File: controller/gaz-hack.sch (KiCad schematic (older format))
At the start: 19 parts, among them Q1 Q_NMOS_GSD, U1 OPTO-TRANSISTOR-4

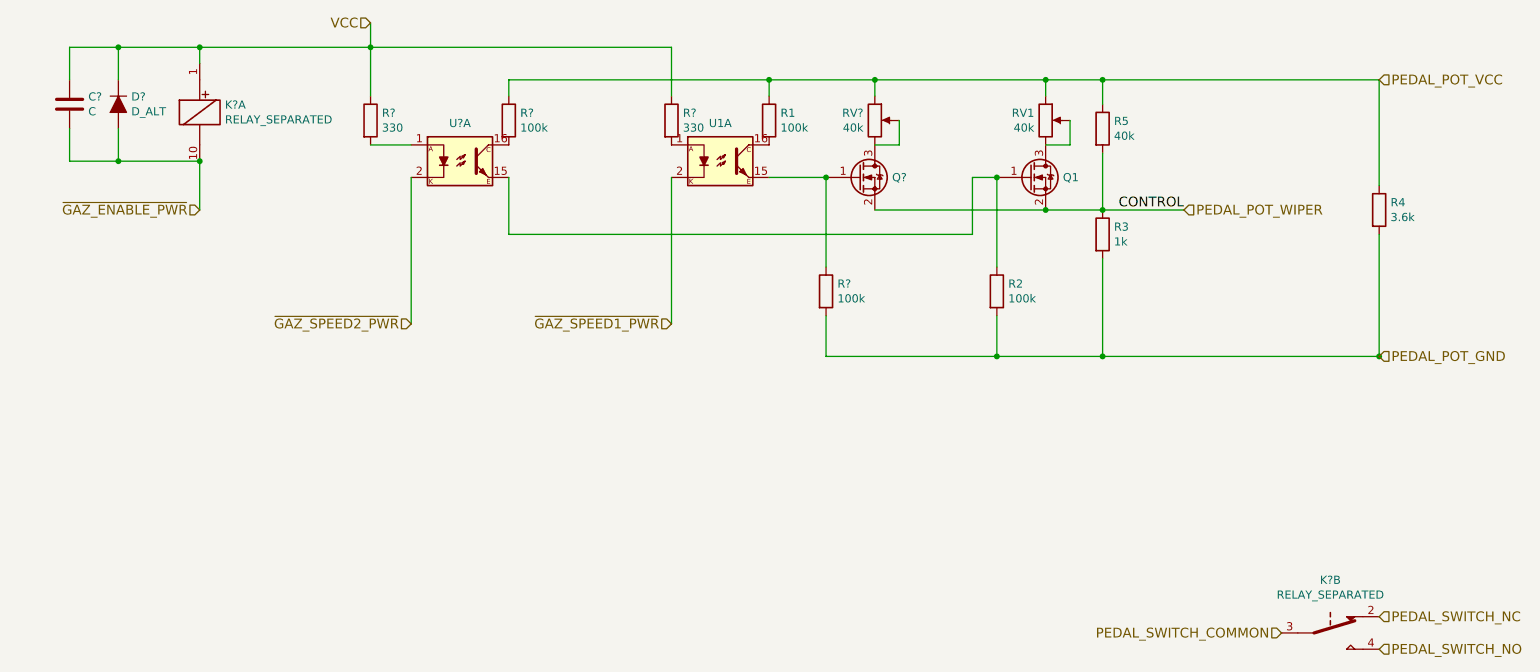
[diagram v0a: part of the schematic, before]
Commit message: Add more stuff to controller, start sourcing parts
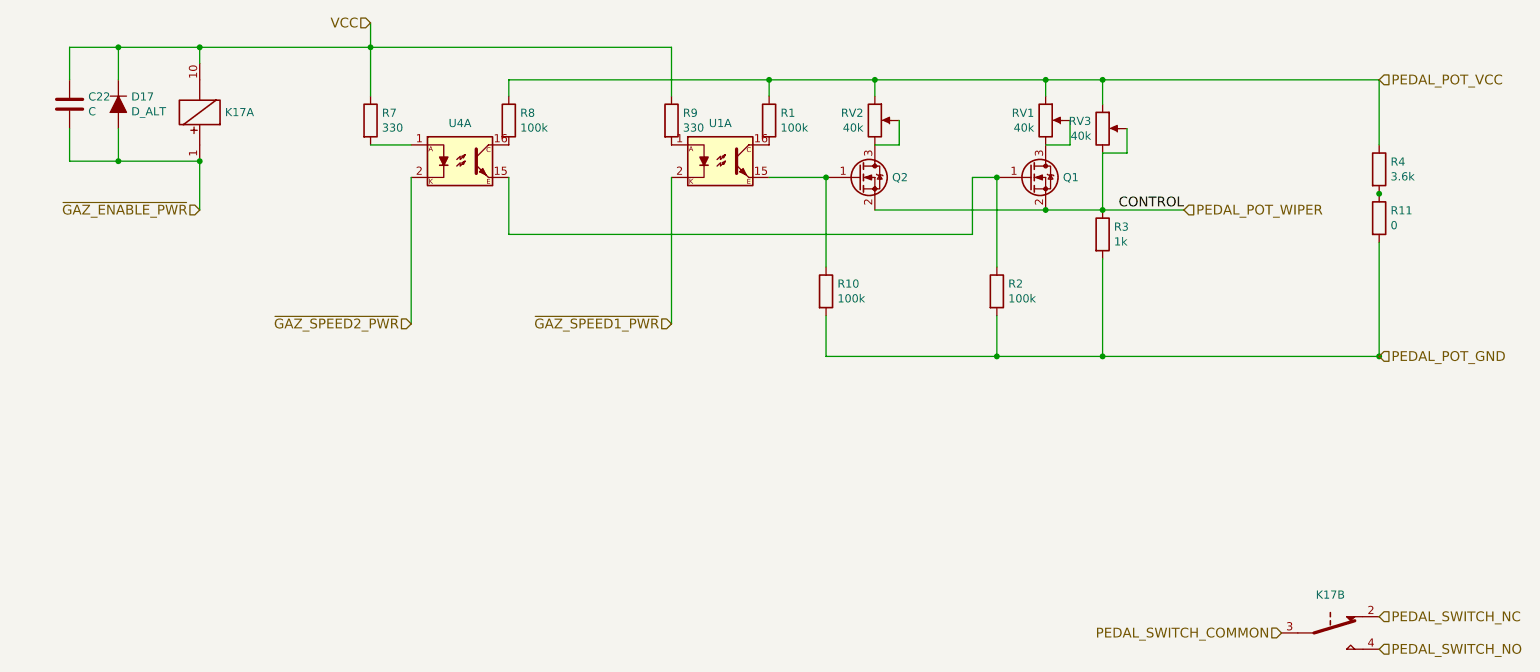
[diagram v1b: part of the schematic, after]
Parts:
- removed R5: 40k, symbol R
- added R11: 0, symbol R
- added RV3: 40k, symbol POT
- gave numbers to parts that had none: 10
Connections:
- net PEDAL_POT_GND: now also R11.2; no longer R4.2
- net PEDAL_POT_VCC: now also RV3.1
- net PEDAL_POT_WIPER: now also RV3.2, RV3.3
- net PEDAL_SWITCH_COMMON: now also K17.3; no longer K17.3
- net PEDAL_SWITCH_NC: now also K17.2; no longer K17.2
- net PEDAL_SWITCH_NO: now also K17.4; no longer K17.4
- net VCC: now also K17.10; no longer K17.1
- net ~GAZ_ENABLE_PWR: now also K17.1; no longer K17.10
- new net: R11.1, R4.2
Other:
- moved on the sheet: R4
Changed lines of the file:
@@
 LIBS:mic-parts
 LIBS:controller-cache
-LIBS:line-interface-cache
 EELAYER 26 0
 EELAYER END
 $Descr A4 11693 8268
 encoding utf-8
-Sheet 3 6
+Sheet 6 10
 Title ""
 Date ""
@@
 L R R4
 U 1 1 58BEE596
-P 9950 2400
-F 0 "R4" H 10020 2446 50  0000 L CNN
-F 1 "3.6k" H 10020 2355 50  0000 L CNN
-F 2 "" V 5480 -500 50  0001 C CNN
-F 3 "" H 5550 -500 50  0001 C CNN
-	1    9950 2400
-	1    0    0    -1
-$EndComp
-Wire Wire Line
-	9950 1600 9950 2250
-Wire Wire Line
-	9950 3300 9950 2550
+P 9950 2150
+F 0 "R4" H 10020 2196 50  0000 L CNN
+F 1 "3.6k" H 10020 2105 50  0000 L CNN
+F 2 "" V 5480 -750 50  0001 C CNN
+F 3 "" H 5550 -750 50  0001 C CNN
+	1    9950 2150
+	1    0    0    -1
+$EndComp
+Wire Wire Line
+	9950 1600 9950 2000
 $Comp
 L OPTO-TRANSISTOR-4 U1
@@
 Connection ~ 7900 1600
 Connection ~ 7600 2200
-$Comp
-L R R5
-U 1 1 58BEEDC4
-P 8250 1900
-F 0 "R5" H 8320 1946 50  0000 L CNN
-F 1 "40k" H 8320 1855 50  0000 L CNN
-F 2 "" V 3780 -1000 50  0001 C CNN
-F 3 "" H 3850 -1000 50  0001 C CNN
-	1    8250 1900
-	1    0    0    -1
-$EndComp
 Wire Wire Line
 	8250 1750 8250 1600
@@
 Connection ~ 8250 3300
 $Comp
-L Q_NMOS_GSD Q?
+L Q_NMOS_GSD Q2
 U 1 1 58C00A06
 P 6750 2200
-F 0 "Q?" H 6956 2200 50  0000 L CNN
+F 0 "Q2" H 6956 2200 50  0000 L CNN
 F 1 "Q_NMOS_GSD" H 6955 2155 50  0001 L CNN
 F 2 "" H 2950 -400 50  0001 C CNN
@@
 $EndComp
 $Comp
-L POT RV?
+L POT RV2
 U 1 1 58C00A0C
 P 6850 1850
-F 0 "RV?" H 6780 1896 50  0000 R CNN
+F 0 "RV2" H 6780 1896 50  0000 R CNN
 F 1 "40k" H 6780 1805 50  0000 R CNN
 F 2 "" H 2700 -450 50  0001 C CNN
@@
 	6850 1600 6850 1700
 $Comp
-L R R?
+L R R10
 U 1 1 58C00A17
 P 6550 2900
-F 0 "R?" H 6620 2946 50  0000 L CNN
+F 0 "R10" H 6620 2946 50  0000 L CNN
 F 1 "100k" H 6620 2855 50  0000 L CNN
 F 2 "" V 2080 0   50  0001 C CNN
@@
 Connection ~ 7600 3300
 $Comp
-L OPTO-TRANSISTOR-4 U?
+L OPTO-TRANSISTOR-4 U4
 U 1 1 58C01026
 P 4300 2100
-F 0 "U?" H 4300 2333 50  0000 C CNN
+F 0 "U4" H 4300 2333 50  0000 C CNN
 F 1 "OPTO-TRANSISTOR-4" H 4300 2334 50  0001 C CNN
 F 2 "" H -350 -1050 50  0001 L CIN
@@
 $EndComp
 $Comp
-L R R?
+L R R8
 U 1 1 58C01078
 P 4600 1850
-F 0 "R?" H 4670 1896 50  0000 L CNN
+F 0 "R8" H 4670 1896 50  0000 L CNN
 F 1 "100k" H 4670 1805 50  0000 L CNN
 F 2 "" V 130 -1050 50  0001 C CNN
@@
 PEDAL_SWITCH_NO
 $Comp
-L RELAY_SEPARATED K?
-U 1 1 58C01F4B
-P 2700 1800
-F 0 "K?" H 2855 1846 50  0000 L CNN
-F 1 "RELAY_SEPARATED" H 2855 1755 50  0000 L CNN
-F 2 "" H -4950 -2500 50  0000 C CNN
-F 3 "" H -4950 -2500 50  0000 C CNN
-	1    2700 1800
-	1    0    0    -1
-$EndComp
-$Comp
-L RELAY_SEPARATED K?
-U 2 1 58C01FFF
+L RELAY_SEPARATED K17
+U 2 1 58C01F4B
 P 9650 5000
-F 0 "K?" V 9325 5000 50  0000 C CNN
-F 1 "RELAY_SEPARATED" V 9416 5000 50  0000 C CNN
-F 2 "" H 4550 400 50  0000 C CNN
-F 3 "" H 4550 400 50  0000 C CNN
-F 4 "?" H 9650 5000 60  0001 C CNN "PartNo"
-F 5 "?" H 9650 5000 60  0001 C CNN "Manufacturer"
-F 6 "?" H 9650 5000 60  0001 C CNN "Distributor"
+F 0 "K17" V 9416 5000 50  0000 C CNN
+F 1 "RELAY_SEPARATED" H 9805 4955 50  0001 L CNN
+F 2 "" H 2000 700 50  0000 C CNN
+F 3 "" H 2000 700 50  0000 C CNN
 	2    9650 5000
 	0    1    1    0
 $EndComp
+$Comp
+L RELAY_SEPARATED K17
+U 1 1 58C01FFF
+P 2700 1800
+F 0 "K17" H 2545 1800 50  0000 R CNN
+F 1 "RELAY_SEPARATED" V 2466 1800 50  0001 C CNN
+F 2 "" H -2400 -2800 50  0000 C CNN
+F 3 "" H -2400 -2800 50  0000 C CNN
+F 4 "?" H 2700 1800 60  0001 C CNN "PartNo"
+F 5 "?" H 2700 1800 60  0001 C CNN "Manufacturer"
+F 6 "?" H 2700 1800 60  0001 C CNN "Distributor"
+	1    2700 1800
+	-1   0    0    1
+$EndComp
 Text HLabel 4000 3100 0    60   Input ~ 0
 ~GAZ_SPEED2_PWR
@@
 Connection ~ 3750 1400
 $Comp
-L R R?
+L R R7
 U 1 1 58C023B7
 P 3750 1850
-F 0 "R?" H 3820 1896 50  0000 L CNN
+F 0 "R7" H 3820 1896 50  0000 L CNN
 F 1 "330" H 3820 1805 50  0000 L CNN
 F 2 "" V -720 -1050 50  0001 C CNN
@@
 $EndComp
 $Comp
-L R R?
+L R R9
 U 1 1 58C024A6
 P 5600 1850
-F 0 "R?" H 5670 1896 50  0000 L CNN
+F 0 "R9" H 5670 1896 50  0000 L CNN
 F 1 "330" H 5670 1805 50  0000 L CNN
 F 2 "" V 1130 -1050 50  0001 C CNN
@@
 	3750 1250 3750 1700
 $Comp
-L D_ALT D?
+L D_ALT D17
 U 1 1 58C0A9F4
 P 2200 1750
-F 0 "D?" V 2154 1671 50  0000 R CNN
+F 0 "D17" V 2154 1671 50  0000 R CNN
 F 1 "D_ALT" V 2245 1671 50  0000 R CNN
 F 2 "" H -2700 -550 50  0001 C CNN
@@
 Connection ~ 2700 2100
 $Comp
-L C C?
+L C C22
 U 1 1 58C0ABFE
 P 1900 1750
-F 0 "C?" H 2015 1796 50  0000 L CNN
+F 0 "C22" H 2015 1796 50  0000 L CNN
 F 1 "C" H 2015 1705 50  0000 L CNN
 F 2 "" H -62 -200 50  0001 C CNN
@@
 Connection ~ 2200 2100
 Connection ~ 2200 1400
+$Comp
+L POT RV3
+U 1 1 58C42214
+P 8250 1900
+F 0 "RV3" H 8180 1946 50  0000 R CNN
+F 1 "40k" H 8180 1855 50  0000 R CNN
+F 2 "" H 4100 -400 50  0001 C CNN
+F 3 "" H 4100 -400 50  0001 C CNN
+	1    8250 1900
+	1    0    0    -1
+$EndComp
+Wire Wire Line
+	8250 2050 8400 2050
+Wire Wire Line
+	8400 2050 8400 1900
+$Comp
+L R R11
+U 1 1 58C42979
+P 9950 2450
+F 0 "R11" H 10020 2496 50  0000 L CNN
+F 1 "0" H 10020 2405 50  0000 L CNN
+F 2 "" V 5480 -450 50  0001 C CNN
+F 3 "" H 5550 -450 50  0001 C CNN
+	1    9950 2450
+	1    0    0    -1
+$EndComp
+Wire Wire Line
+	9950 3300 9950 2600
+Connection ~ 9950 2300
 $EndSCHEMATC

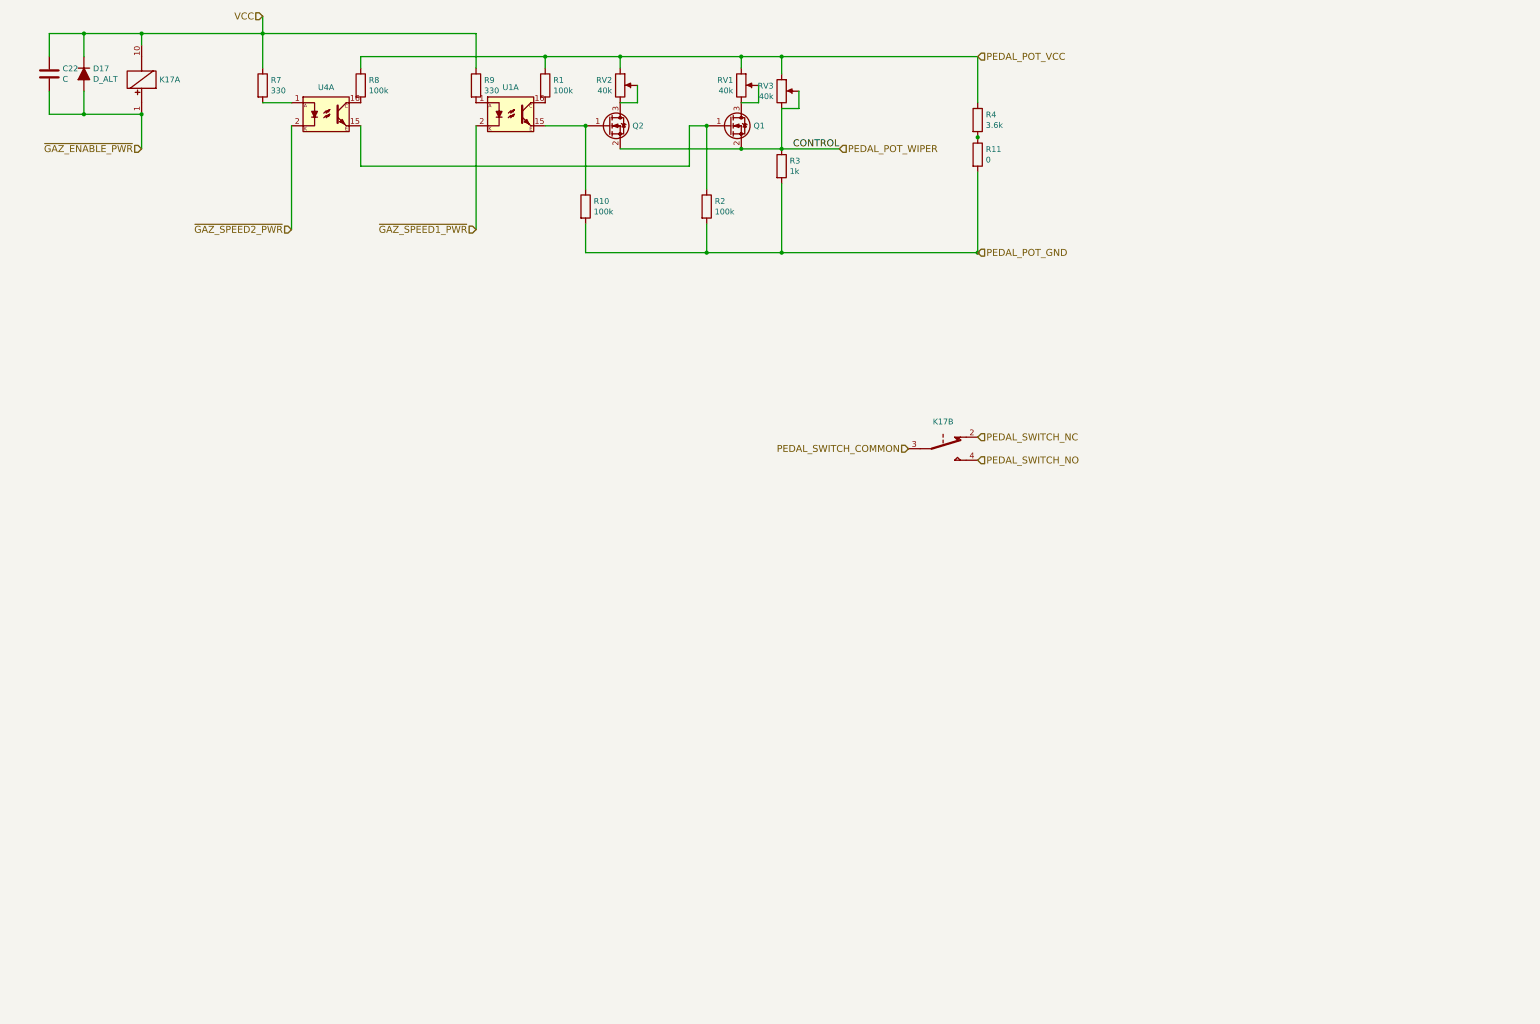
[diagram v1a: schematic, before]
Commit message: Change gas pedal interface so that it supports going up and down from the middle voltage so that it's compatible with Linde forklift gas mechanism
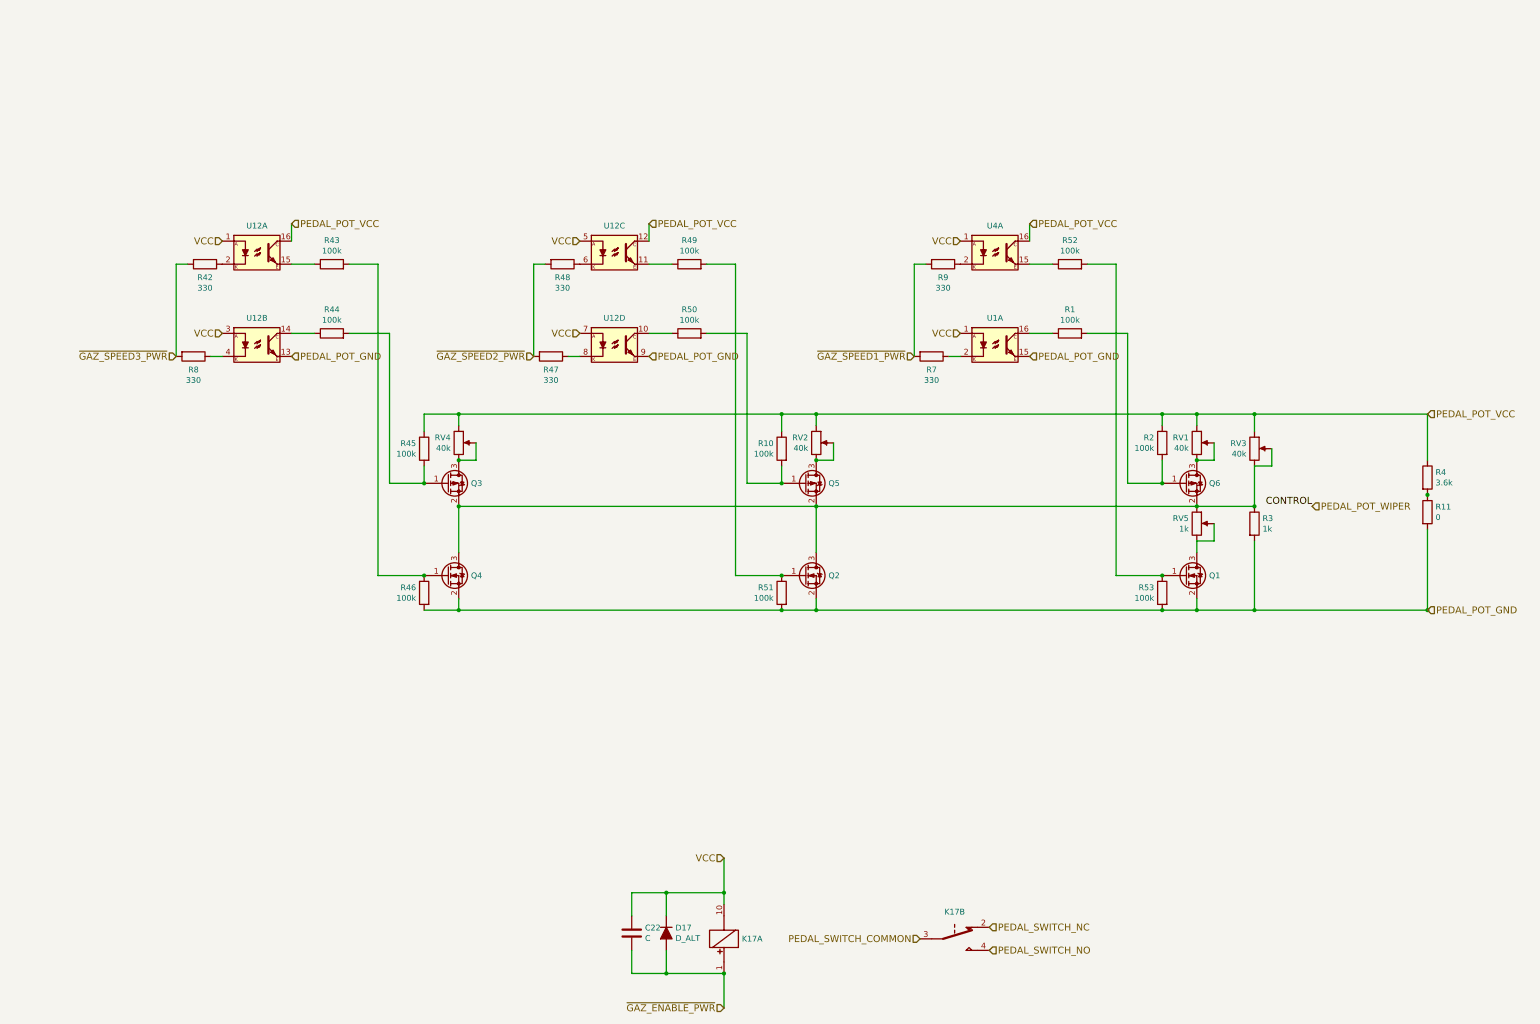
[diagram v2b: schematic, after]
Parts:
- added Q3, Q5, Q6: Q_PMOS_GSD, symbol Q_PMOS_GSD
- added Q4: Q_NMOS_GSD, Housings_SOT-23_SOT-143_TSOT-6:SOT-23_Handsoldering, symbol Q_NMOS_GSD
- added R42, R47, R48: 330, Resistors_SMD:R_0603_HandSoldering, symbol R
- added R43, R44, R45, R46, R49, R50, R51, R52, R53: 100k, Resistors_SMD:R_0603_HandSoldering, symbol R
- added RV4: 40k, symbol POT
- added RV5: 1k, symbol POT
- added U12: OPTO-TRANSISTOR-4, symbol OPTO-TRANSISTOR-4
- C22: footprint (none) -> Capacitors_SMD:C_0603_HandSoldering
- D17: footprint (none) -> Diodes_SMD:D_SOD-123
- K17: footprint (none) -> smalsiukas-footpints:Relay_SPDT
- Q1, Q2: footprint (none) -> Housings_SOT-23_SOT-143_TSOT-6:SOT-23_Handsoldering
- R1, R10, R11, R2, R3, R4, R7, R9: footprint (none) -> Resistors_SMD:R_0603_HandSoldering
- R8: value 100k -> 330; footprint (none) -> Resistors_SMD:R_0603_HandSoldering
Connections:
- net PEDAL_POT_GND: now also Q1.2 (S), Q2.2 (S), U1.15, Q4.2 (S), R46.2, R51.2, R53.2, U12.13, U12.9; no longer R10.2, R2.2
- net PEDAL_POT_VCC: now also R10.1, R2.1, U4.16, R45.1, RV4.1, U12.12, U12.16; no longer R1.1, R8.1
- net PEDAL_POT_WIPER: no longer Q1.2 (S), Q2.2 (S), R3.1, RV3.2, RV3.3
- net VCC: now also U1.1, U4.1, U12.1, U12.3, U12.5, U12.7; no longer R7.1, R9.1
- net ~GAZ_SPEED1_PWR: now also R7.2, R9.2; no longer U1.2
- net ~GAZ_SPEED2_PWR: now also R47.2, R48.2; no longer U4.2
- net at U1.16: now also R1.1; no longer R1.2
- net at RV1.2, RV1.3: now also Q6.3 (D); no longer Q1.3 (D)
- net at RV2.2, RV2.3: now also Q5.3 (D); no longer Q2.3 (D)
- net ~GAZ_SPEED3_PWR: now reaches R8.2
- net ~GAZ_SPEED3_PWR: now also R42.2; no longer U4.16
- new net: R7.1, U1.2
- new net: Q2.3 (D), Q3.2 (S), Q4.3 (D), Q5.2 (S), Q6.2 (S), R3.1, RV3.2, RV3.3, RV5.1
- new net: Q1.1 (G), R52.2, R53.1
- new net: Q1.3 (D), RV5.2, RV5.3
- new net: Q6.1 (G), R1.2, R2.2
- new net: Q2.1 (G), R49.2, R51.1
- new net: Q5.1 (G), R10.2, R50.2
- new net: R52.1, U4.15
- new net: R9.1, U4.2
- new net: Q4.1 (G), R43.2, R46.1
- new net: Q3.3 (D), RV4.2, RV4.3
- new net: Q3.1 (G), R44.2, R45.2
- new net: R50.1, U12.10
- new net: R47.1, U12.8
- new net: R49.1, U12.11
- new net: R48.1, U12.6
- new net: R44.1, U12.14
- new net: R8.1, U12.4
- new net: R43.1, U12.15
- new net: R42.1, U12.2
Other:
- moved on the sheet: C22, D17, K17A, K17B, Q1, Q2, R1, R10, R11, R2, R3, R4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
